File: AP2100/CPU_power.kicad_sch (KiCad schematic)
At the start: 193 parts

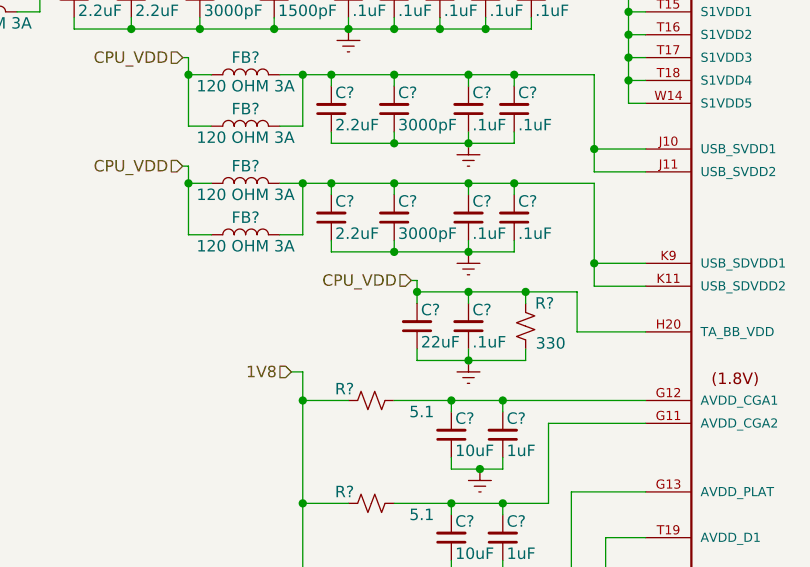
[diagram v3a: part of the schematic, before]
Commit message: Finish reset section
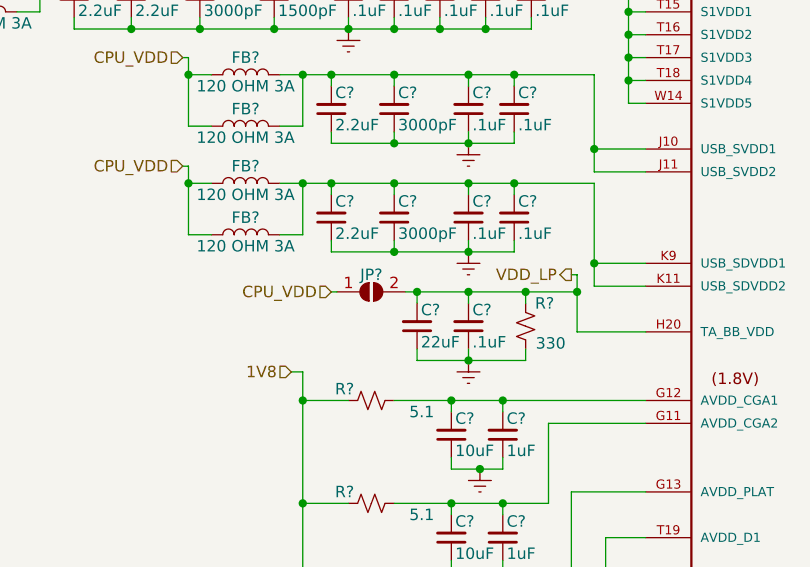
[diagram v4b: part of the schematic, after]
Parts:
- added JP?: SolderJumper_2_Open, symbol Jumper:SolderJumper_2_Open
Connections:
- net CPU_VDD: now also JP?.1 (A); no longer C?.2, C?.2, R?.2, U?.H20 (TA_BB_VDD)
- new net VDD_LP: C?.2, C?.2, JP?.2 (B), R?.2, U?.H20 (TA_BB_VDD)
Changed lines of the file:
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@@
 (kicad_sch (version 20200828) (generator eeschema)
-  (page 5 9)
+  (page 6 10)
   (paper "A3")
   (junction (at 31.115 177.165) (diameter 0.9144) (color 0 0 0 0))
@@
   (junction (at 97.79 213.995) (diameter 0.9144) (color 0 0 0 0))
   (junction (at 98.425 177.165) (diameter 0.9144) (color 0 0 0 0))
+  (junction (at 103.505 213.995) (diameter 0.9144) (color 0 0 0 0))
   (junction (at 105.41 177.165) (diameter 0.9144) (color 0 0 0 0))
   (junction (at 105.41 198.12) (diameter 0.9144) (color 0 0 0 0))
@@
     (stroke (width 0) (type solid) (color 0 0 0 0))
   )
+  (wire (pts (xy 76.2 213.995) (xy 76.835 213.995))
+    (stroke (width 0) (type solid) (color 0 0 0 0))
+  )
   (wire (pts (xy 78.105 177.165) (xy 78.105 178.435))
     (stroke (width 0) (type solid) (color 0 0 0 0))
@@
     (stroke (width 0) (type solid) (color 0 0 0 0))
   )
-  (wire (pts (xy 85.09 212.725) (xy 85.725 212.725))
+  (wire (pts (xy 84.455 213.995) (xy 85.725 213.995))
     (stroke (width 0) (type solid) (color 0 0 0 0))
   )
@@
     (stroke (width 0) (type solid) (color 0 0 0 0))
   )
-  (wire (pts (xy 85.725 212.725) (xy 85.725 213.995))
-    (stroke (width 0) (type solid) (color 0 0 0 0))
-  )
   (wire (pts (xy 85.725 213.995) (xy 91.44 213.995))
     (stroke (width 0) (type solid) (color 0 0 0 0))
@@
     (stroke (width 0) (type solid) (color 0 0 0 0))
   )
+  (wire (pts (xy 102.87 212.09) (xy 103.505 212.09))
+    (stroke (width 0) (type solid) (color 0 0 0 0))
+  )
   (wire (pts (xy 102.87 236.22) (xy 102.87 248.92))
     (stroke (width 0) (type solid) (color 0 0 0 0))
@@
     (stroke (width 0) (type solid) (color 0 0 0 0))
   )
+  (wire (pts (xy 103.505 212.09) (xy 103.505 213.995))
+    (stroke (width 0) (type solid) (color 0 0 0 0))
+  )
   (wire (pts (xy 103.505 213.995) (xy 103.505 218.44))
     (stroke (width 0) (type solid) (color 0 0 0 0))
@@
     (effects (font (size 1.27 1.27)) (justify right))
   )
-  (hierarchical_label "CPU_VDD" (shape input) (at 85.09 212.725 180)
+  (hierarchical_label "CPU_VDD" (shape input) (at 76.2 213.995 180)
+    (effects (font (size 1.27 1.27)) (justify right))
+  )
+  (hierarchical_label "VDD_LP" (shape output) (at 102.87 212.09 180)
     (effects (font (size 1.27 1.27)) (justify right))
   )
@@
       (effects (font (size 1.27 1.27)) hide)
     )
+  )
+  (symbol (lib_id "Jumper:SolderJumper_2_Open") (at 80.645 213.995 0) (unit 1)
+    (in_bom yes) (on_board yes)
+    (property "Reference" "JP?" (id 0) (at 80.645 212.09 0))
+    (property "Value" "SolderJumper_2_Open" (id 1) (at 81.28 210.185 0)
+      (effects (font (size 1.27 1.27)) hide)
+    )
+    (property "Footprint" "" (id 2) (at 80.645 213.995 0)
+      (effects (font (size 1.27 1.27)) hide)
+    )
+    (property "Datasheet" "~" (id 3) (at 80.645 213.995 0)
+      (effects (font (size 1.27 1.27)) hide)
+    )

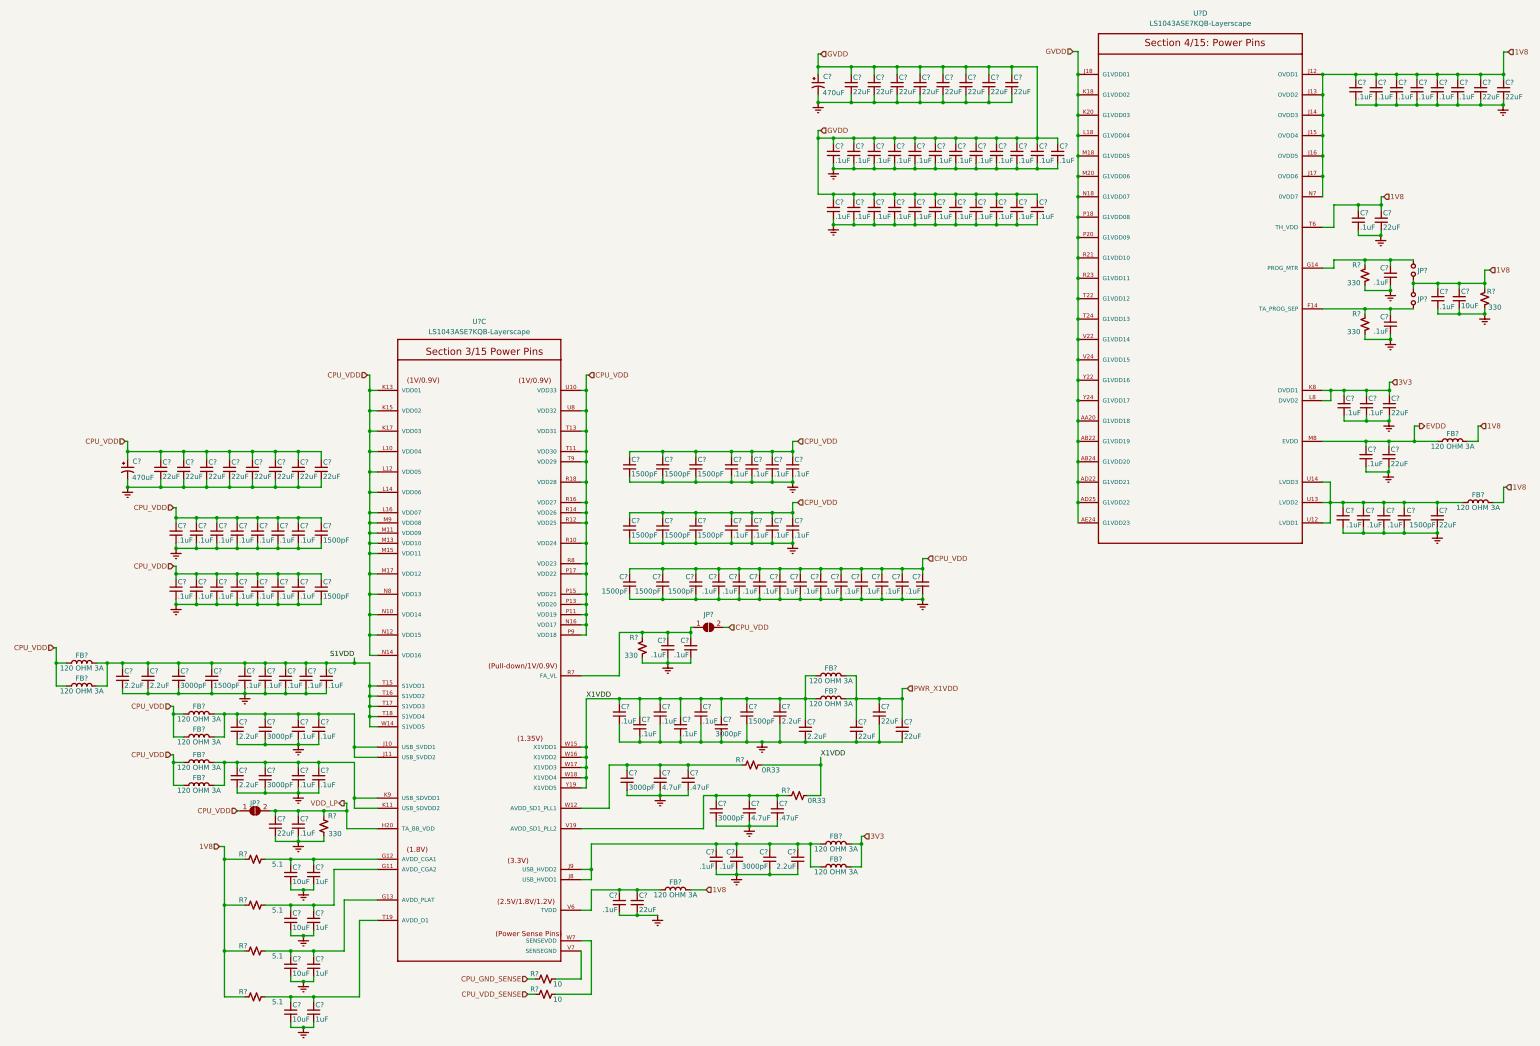
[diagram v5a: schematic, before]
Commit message: Annotate and update PCB with current design
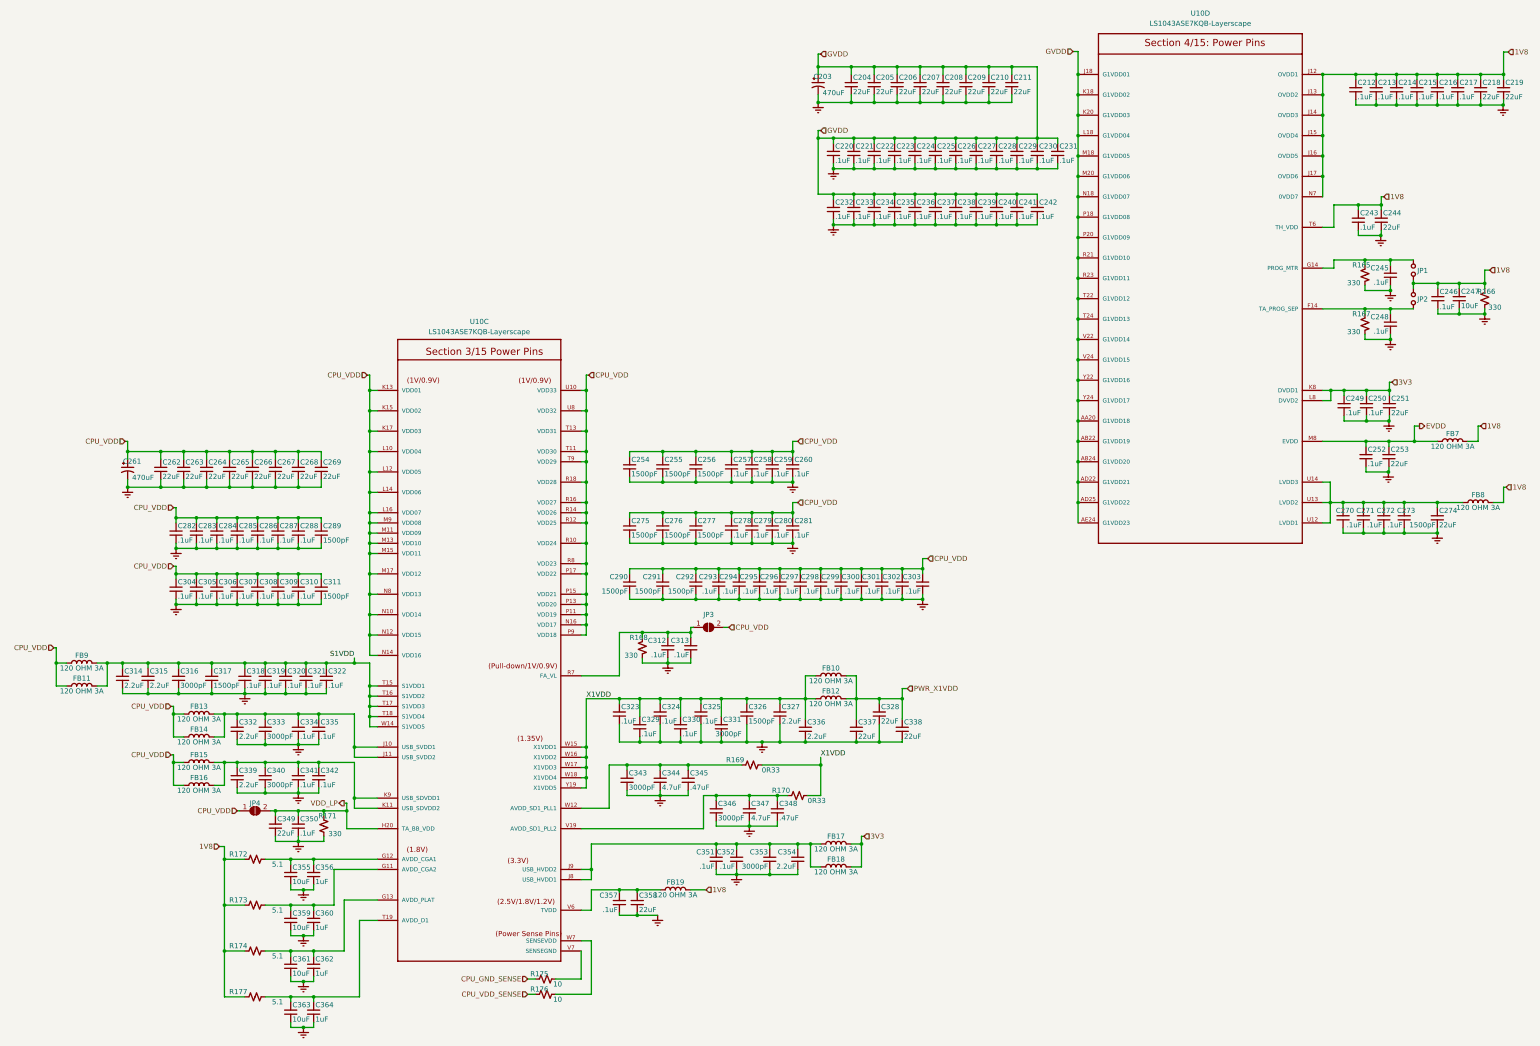
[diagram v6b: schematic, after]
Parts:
- gave numbers to parts that had none: 193

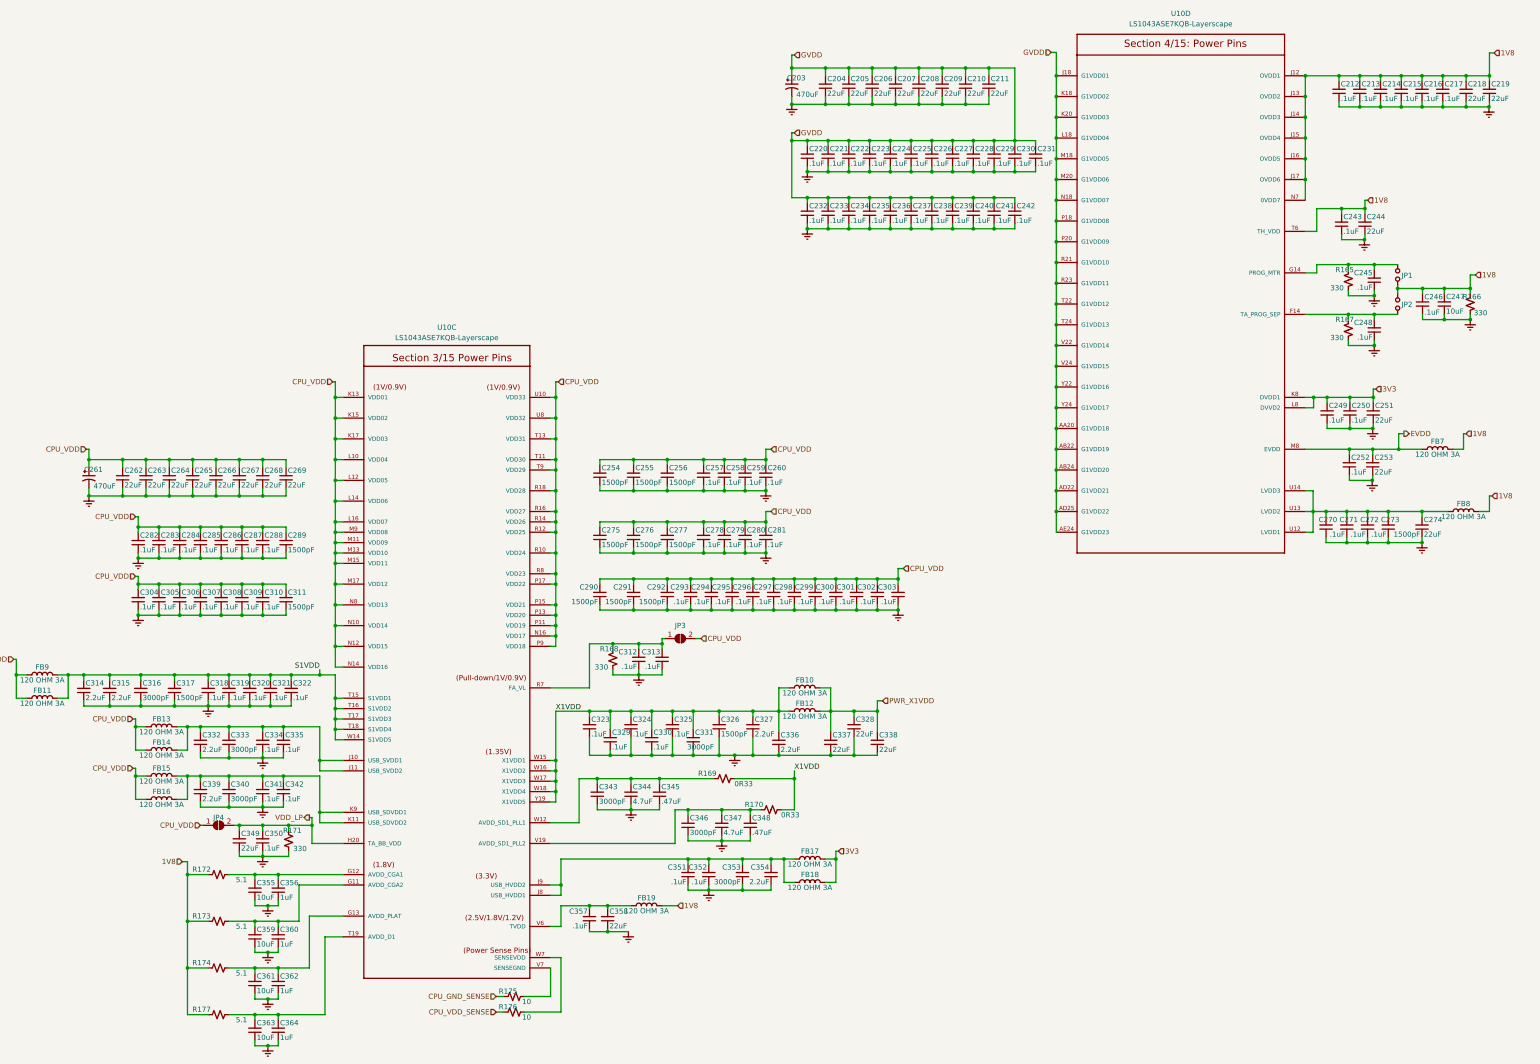
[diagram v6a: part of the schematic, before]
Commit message: Review / cleanup footprints, etc
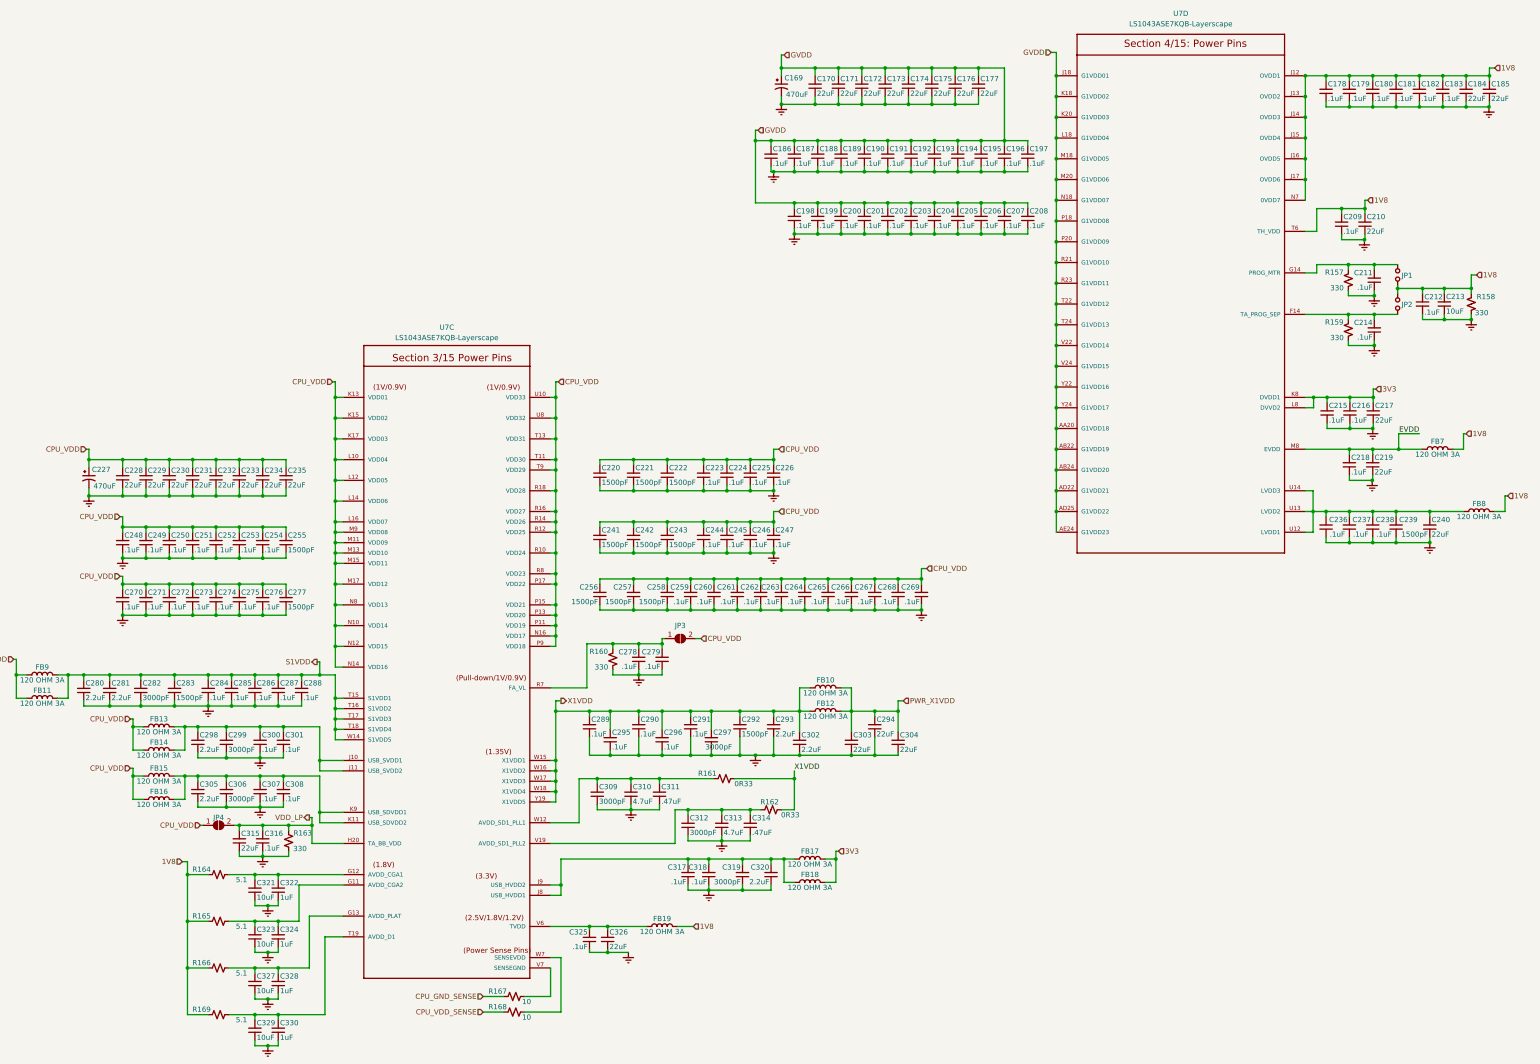
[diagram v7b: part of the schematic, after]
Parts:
- JP1, JP2, JP3, JP4: footprint (none) -> Jumper:SolderJumper-2_P1.3mm_Open_TrianglePad1.0x1.5mm
- renumbered C203 to C169, C204 to C170, C205 to C171, C206 to C172, C207 to C173, C208 to C174, C209 to C175, C210 to C176, C211 to C177, C212 to C178, C213 to C179, C214 to C180, C215 to C181, C216 to C182, C217 to C183, C218 to C184, C219 to C185, C220 to C186, C221 to C187, C222 to C188, C223 to C189, C224 to C190, C225 to C191, C226 to C192, C227 to C193, C228 to C194, C229 to C195, C230 to C196, C231 to C197, C232 to C198, C233 to C199, C234 to C200, C235 to C201, C236 to C202, C237 to C203, C238 to C204, C239 to C205, C240 to C206, C241 to C207, C242 to C208, C243 to C209, C244 to C210, C245 to C211, C246 to C212, C247 to C213, C248 to C214, C249 to C215, C250 to C216, C251 to C217, C252 to C218, C253 to C219, C254 to C220, C255 to C221, C256 to C222, C257 to C223, C258 to C224, C259 to C225, C260 to C226, C261 to C227, C262 to C228, C263 to C229, C264 to C230, C265 to C231, C266 to C232, C267 to C233, C268 to C234, C269 to C235, C270 to C236, C271 to C237, C272 to C238, C273 to C239, C274 to C240, C275 to C241, C276 to C242, C277 to C243, C278 to C244, C279 to C245, C280 to C246, C281 to C247, C282 to C248, C283 to C249, C284 to C250, C285 to C251, C286 to C252, C287 to C253, C288 to C254, C289 to C255, C290 to C256, C291 to C257, C292 to C258, C293 to C259, C294 to C260, C295 to C261, C296 to C262, C297 to C263, C298 to C264, C299 to C265, C300 to C266, C301 to C267, C302 to C268, C303 to C269, C304 to C270, C305 to C271, C306 to C272, C307 to C273, C308 to C274, C309 to C275, C310 to C276, C311 to C277, C312 to C278, C313 to C279, C314 to C280, C315 to C281, C316 to C282, C317 to C283, C318 to C284, C319 to C285, C320 to C286, C321 to C287, C322 to C288, C323 to C289, C324 to C290, C325 to C291, C326 to C292, C327 to C293, C328 to C294, C329 to C295, C330 to C296, C331 to C297, C332 to C298, C333 to C299, C334 to C300, C335 to C301, C336 to C302, C337 to C303, C338 to C304, C339 to C305, C340 to C306, C341 to C307, C342 to C308, C343 to C309, C344 to C310, C345 to C311, C346 to C312, C347 to C313, C348 to C314, C349 to C315, C350 to C316, C351 to C317, C352 to C318, C353 to C319, C354 to C320, C355 to C321, C356 to C322, C359 to C323, C360 to C324, C357 to C325, C358 to C326, C361 to C327, C362 to C328, C363 to C329, C364 to C330, R165 to R157, R166 to R158, R167 to R159, R168 to R160, R169 to R161, R170 to R162, R171 to R163, R172 to R164, R173 to R165, R174 to R166, R175 to R167, R176 to R168, R177 to R169, U10 to U7
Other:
- moved on the sheet: C169, C170, C171, C172, C173, C174, C175, C176, C177, C178, C179, C180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

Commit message: Added antenna mounting holes
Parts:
- renumbered R157 to R154, R158 to R155, R159 to R156, R160 to R157, R161 to R158, R162 to R159, R163 to R160, R164 to R161, R165 to R162, R166 to R163, R167 to R164, R168 to R165, R169 to R166
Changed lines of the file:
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@@
   (symbol (lib_id "Device:R_Small_US") (at 80.645 226.06 90) (unit 1)
     (in_bom yes) (on_board yes)
-    (property "Reference" "R164" (id 0) (at 78.74 224.79 90)
+    (property "Reference" "R161" (id 0) (at 78.74 224.79 90)
       (effects (font (size 1.27 1.27)) (justify left))
     )
@@
   (symbol (lib_id "Device:R_Small_US") (at 80.645 237.49 90) (unit 1)
     (in_bom yes) (on_board yes)
-    (property "Reference" "R165" (id 0) (at 78.74 236.22 90)
+    (property "Reference" "R162" (id 0) (at 78.74 236.22 90)
       (effects (font (size 1.27 1.27)) (justify left))
     )
@@
   (symbol (lib_id "Device:R_Small_US") (at 80.645 248.92 90) (unit 1)
     (in_bom yes) (on_board yes)
-    (property "Reference" "R166" (id 0) (at 78.74 247.65 90)
+    (property "Reference" "R163" (id 0) (at 78.74 247.65 90)
       (effects (font (size 1.27 1.27)) (justify left))
     )
@@
   (symbol (lib_id "Device:R_Small_US") (at 80.645 260.35 90) (unit 1)
     (in_bom yes) (on_board yes)
-    (property "Reference" "R169" (id 0) (at 78.74 259.08 90)
+    (property "Reference" "R166" (id 0) (at 78.74 259.08 90)
       (effects (font (size 1.27 1.27)) (justify left))
     )
@@
   (symbol (lib_id "Device:R_Small_US") (at 97.79 217.805 180) (unit 1)
     (in_bom yes) (on_board yes)
-    (property "Reference" "R163" (id 0) (at 103.505 215.9 0)
+    (property "Reference" "R160" (id 0) (at 103.505 215.9 0)
       (effects (font (size 1.27 1.27)) (justify left))
     )
@@
   (symbol (lib_id "Device:R_Small_US") (at 153.035 255.905 270) (unit 1)
     (in_bom yes) (on_board yes)
-    (property "Reference" "R167" (id 0) (at 146.685 254.635 90)
+    (property "Reference" "R164" (id 0) (at 146.685 254.635 90)
       (effects (font (size 1.27 1.27)) (justify left))
     )
@@
   (symbol (lib_id "Device:R_Small_US") (at 153.035 259.715 270) (unit 1)
     (in_bom yes) (on_board yes)
-    (property "Reference" "R168" (id 0) (at 146.685 258.445 90)
+    (property "Reference" "R165" (id 0) (at 146.685 258.445 90)
       (effects (font (size 1.27 1.27)) (justify left))
     )
@@
   (symbol (lib_id "Device:R_Small_US") (at 177.165 173.355 0) (mirror x) (unit 1)
     (in_bom yes) (on_board yes)
-    (property "Reference" "R160" (id 0) (at 171.45 171.45 0)
+    (property "Reference" "R157" (id 0) (at 171.45 171.45 0)
       (effects (font (size 1.27 1.27)) (justify left))
     )
@@
   (symbol (lib_id "Device:R_Small_US") (at 204.47 202.565 90) (unit 1)
     (in_bom yes) (on_board yes)
-    (property "Reference" "R161" (id 0) (at 202.565 201.295 90)
+    (property "Reference" "R158" (id 0) (at 202.565 201.295 90)
       (effects (font (size 1.27 1.27)) (justify left))
     )
@@
   (symbol (lib_id "Device:R_Small_US") (at 215.9 210.185 90) (unit 1)
     (in_bom yes) (on_board yes)
-    (property "Reference" "R162" (id 0) (at 217.805 208.28 90)
+    (property "Reference" "R159" (id 0) (at 217.805 208.28 90)
       (effects (font (size 1.27 1.27)) (justify left))
     )
@@
   (symbol (lib_id "Device:R_Small_US") (at 357.251 80.518 0) (mirror x) (unit 1)
     (in_bom yes) (on_board yes)
-    (property "Reference" "R157" (id 0) (at 351.536 78.613 0)
+    (property "Reference" "R154" (id 0) (at 351.536 78.613 0)
       (effects (font (size 1.27 1.27)) (justify left))
     )
@@
   (symbol (lib_id "Device:R_Small_US") (at 357.251 92.71 0) (mirror x) (unit 1)
     (in_bom yes) (on_board yes)
-    (property "Reference" "R159" (id 0) (at 351.536 90.805 0)
+    (property "Reference" "R156" (id 0) (at 351.536 90.805 0)
       (effects (font (size 1.27 1.27)) (justify left))
     )
@@
   (symbol (lib_id "Device:R_Small_US") (at 387.35 86.36 0) (mirror y) (unit 1)
     (in_bom yes) (on_board yes)
-    (property "Reference" "R158" (id 0) (at 393.192 84.582 0)
-      (effects (font (size 1.27 1.27)) (justify left))
-    )
+    (property "Reference" "R155" (id 0) (at 393.192 84.582 0)
+      (effects (font (size 1.27 1.27)) (justify left))
+    )
